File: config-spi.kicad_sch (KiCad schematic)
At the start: 38 parts, among them J4 0878311420, Q6 BSS138APW, Q7 BSS138APW, U3 XC7K70T-FBG484, U5 S25FL128LAGNFA010

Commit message: Loclib
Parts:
- U5: footprint antmicro-footprints:S25FL128SAGNFI000 -> lpddr4-test-board-footprints:S25FL128SAGNFI000; symbol antmicroMemory:S25FL128LAGNFA010 -> lpddr4-test-board:S25FL128LAGNFA010
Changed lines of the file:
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@@
     )
     (property "Value" "GND" (id 1) (at 23.622 262.2042 0))
-    (property "Footprint" "" (id 2) (at 23.495 257.81 0)
+    (property "Footprint" "lpddr4-test-board-footprints:" (id 2) (at 23.495 257.81 0)
       (effects (font (size 1.27 1.27)) hide)
     )
@@
     )
     (property "Value" "GND" (id 1) (at 70.4342 258.318 0))
-    (property "Footprint" "" (id 2) (at 66.04 258.445 0)
+    (property "Footprint" "lpddr4-test-board-footprints:" (id 2) (at 66.04 258.445 0)
       (effects (font (size 1.27 1.27)) hide)
     )
@@
     )
     (property "Value" "GND" (id 1) (at 69.977 140.2842 0))
-    (property "Footprint" "" (id 2) (at 69.85 135.89 0)
+    (property "Footprint" "lpddr4-test-board-footprints:" (id 2) (at 69.85 135.89 0)
       (effects (font (size 1.27 1.27)) hide)
     )
@@
     )
     (property "Value" "GND" (id 1) (at 235.5342 232.918 0))
-    (property "Footprint" "" (id 2) (at 231.14 233.045 0)
+    (property "Footprint" "lpddr4-test-board-footprints:" (id 2) (at 231.14 233.045 0)
       (effects (font (size 1.27 1.27)) hide)
     )
@@
     )
     (property "Value" "GND" (id 1) (at 235.5342 245.618 0))
-    (property "Footprint" "" (id 2) (at 231.14 245.745 0)
+    (property "Footprint" "lpddr4-test-board-footprints:" (id 2) (at 231.14 245.745 0)
       (effects (font (size 1.27 1.27)) hide)
     )
@@
     )
     (property "Value" "GND" (id 1) (at 166.3192 239.268 0))
-    (property "Footprint" "" (id 2) (at 161.925 239.395 0)
+    (property "Footprint" "lpddr4-test-board-footprints:" (id 2) (at 161.925 239.395 0)
       (effects (font (size 1.27 1.27)) hide)
     )
@@
     )
     (property "Value" "GND" (id 1) (at 166.9542 258.953 0))
-    (property "Footprint" "" (id 2) (at 162.56 259.08 0)
+    (property "Footprint" "lpddr4-test-board-footprints:" (id 2) (at 162.56 259.08 0)
       (effects (font (size 1.27 1.27)) hide)
     )
@@
     )
     (property "Value" "GND" (id 1) (at 249.047 174.5742 0))
-    (property "Footprint" "" (id 2) (at 248.92 170.18 0)
+    (property "Footprint" "lpddr4-test-board-footprints:" (id 2) (at 248.92 170.18 0)
       (effects (font (size 1.27 1.27)) hide)
     )
@@
     )
     (property "Value" "GND" (id 1) (at 156.972 179.0192 0))
-    (property "Footprint" "" (id 2) (at 156.845 174.625 0)
+    (property "Footprint" "lpddr4-test-board-footprints:" (id 2) (at 156.845 174.625 0)
       (effects (font (size 1.27 1.27)) hide)
     )
@@
     )
     (property "Value" "GND" (id 1) (at 236.1692 260.858 0))
-    (property "Footprint" "" (id 2) (at 231.775 260.985 0)
+    (property "Footprint" "lpddr4-test-board-footprints:" (id 2) (at 231.775 260.985 0)
       (effects (font (size 1.27 1.27)) hide)
     )
@@
     )
     (property "Value" "GND" (id 1) (at 282.067 182.1942 0))
-    (property "Footprint" "" (id 2) (at 281.94 177.8 0)
+    (property "Footprint" "lpddr4-test-board-footprints:" (id 2) (at 281.94 177.8 0)
       (effects (font (size 1.27 1.27)) hide)
     )
@@
     )
     (property "Value" "GND" (id 1) (at 133.477 141.5542 0))
-    (property "Footprint" "" (id 2) (at 133.35 137.16 0)
+    (property "Footprint" "lpddr4-test-board-footprints:" (id 2) (at 133.35 137.16 0)
       (effects (font (size 1.27 1.27)) hide)
     )
@@
     )
     (property "Value" "GND" (id 1) (at 376.047 129.4892 0))
-    (property "Footprint" "" (id 2) (at 375.92 125.095 0)
+    (property "Footprint" "lpddr4-test-board-footprints:" (id 2) (at 375.92 125.095 0)
       (effects (font (size 1.27 1.27)) hide)
     )
@@
     )
     (property "Value" "GND" (id 1) (at 61.722 113.6142 0))
-    (property "Footprint" "" (id 2) (at 61.595 109.22 0)
+    (property "Footprint" "lpddr4-test-board-footprints:" (id 2) (at 61.595 109.22 0)
       (effects (font (size 1.27 1.27)) hide)
     )
@@
     (pin "1")
   )
-  (symbol (lib_id "antmicroMemory:S25FL128LAGNFA010") (at 109.22 105.41 0) (mirror y) (unit 1)
+  (symbol (lib_id "lpddr4-test-board:S25FL128LAGNFA010") (at 109.22 105.41 0) (mirror y) (unit 1)
     (in_bom yes) (on_board yes) (fields_autoplaced)
     (property "Reference" "U5" (id 0) (at 91.44 98.7859 0)
@@
       (effects (font (size 1.524 1.524)))
     )
-    (property "Footprint" "antmicro-footprints:S25FL128SAGNFI000" (id 2) (at 90.805 144.78 0)
-      (effects (font (size 1.524 1.524)) hide)
-    )
+    (property "Footprint" "lpddr4-test-board-footprints:S25FL128SAGNFI000" (id 2) (at 90.805 144.78 0)
+      (effects (font (size 1.524 1.524)) hide)
+    )

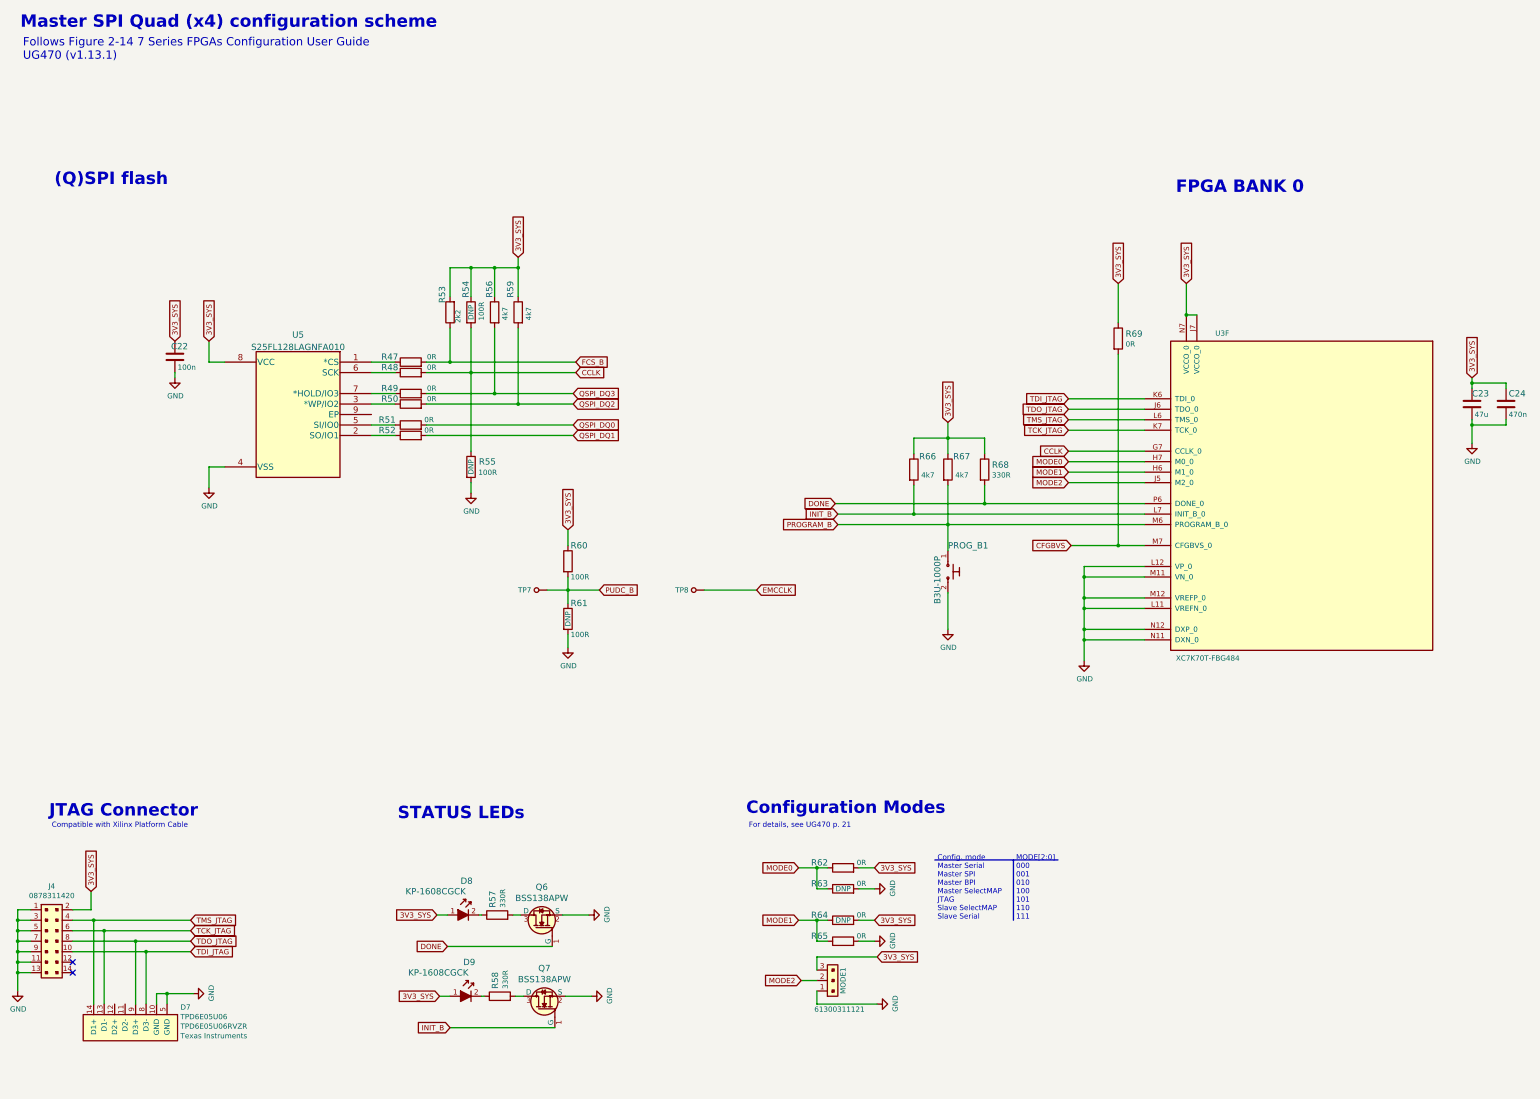
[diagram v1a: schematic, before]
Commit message: Introduce standardized components
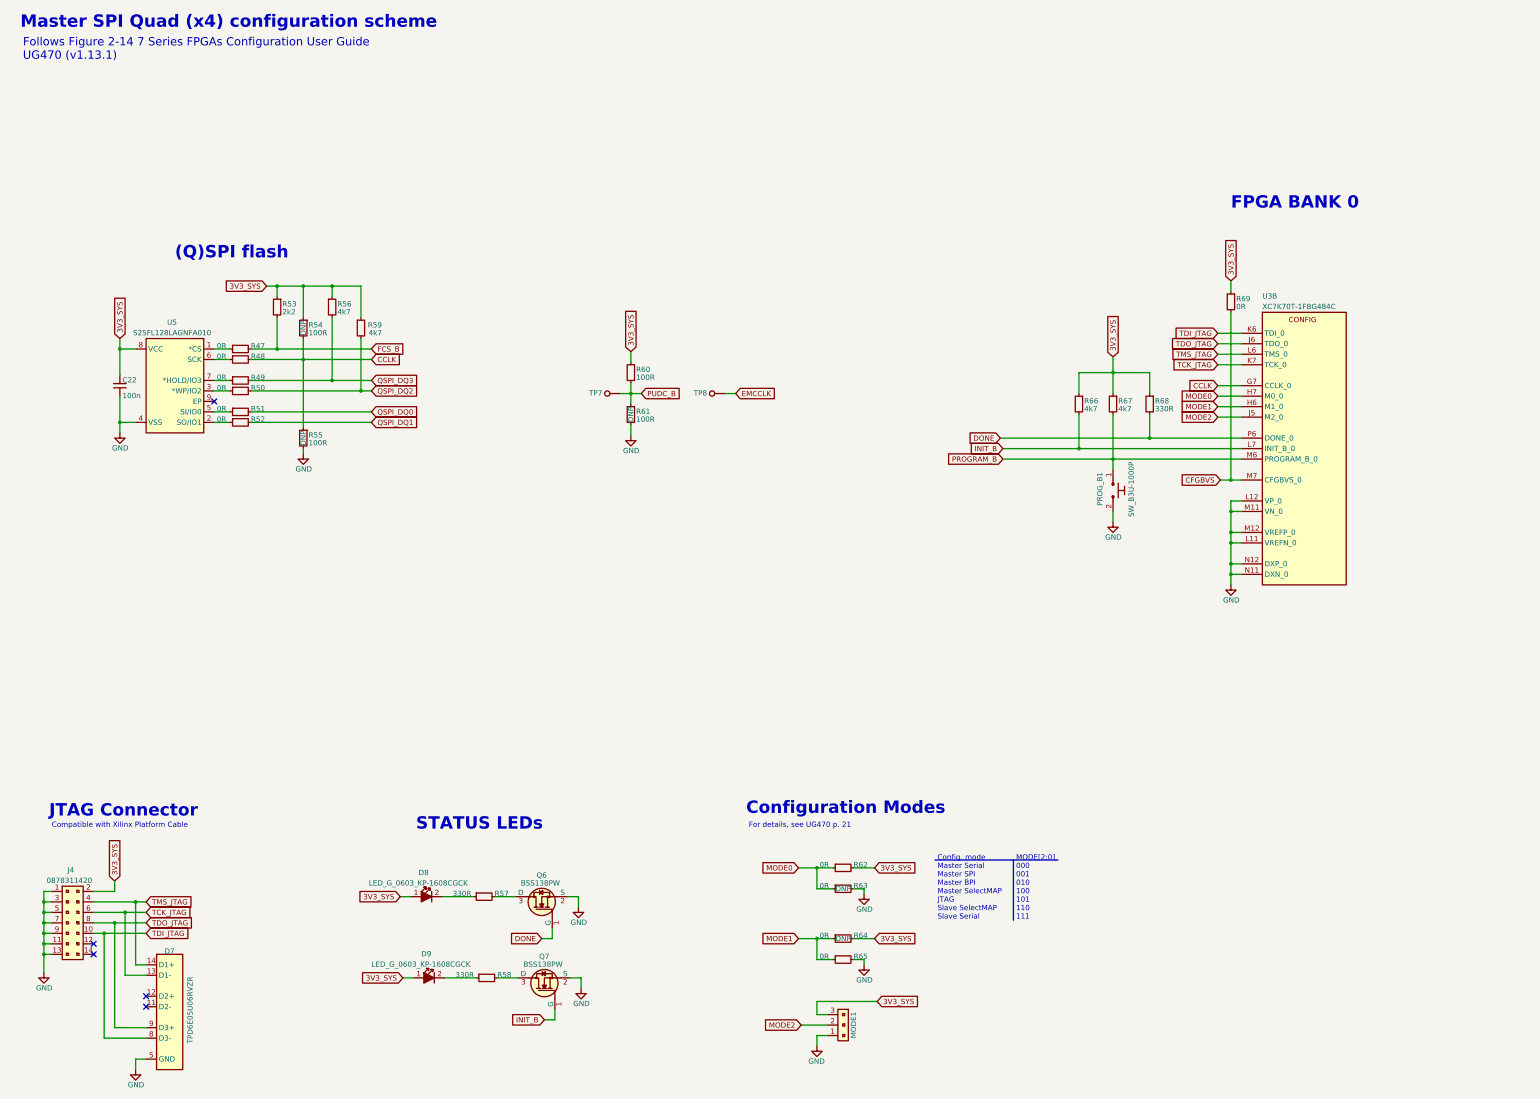
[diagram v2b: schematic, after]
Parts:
- removed C23: C_47u_0603, lpddr4-test-board-footprints:0603-cap, symbol lpddr4-test-board:C_47u_0603
- removed C24: C_470n_0402, lpddr4-test-board-footprints:0402-cap, symbol lpddr4-test-board:C_470n_0402
- removed U3: XC7K70T-FBG484, lpddr4-test-board-footprints:BGA484C100P22X22_2300X2300X244N, symbol lpddr4-test-board:XC7K70T-FBG484
- added U3: XC7K70T-FBG484, lpddr4-test-board-footprints:BGA484C100P22X22_2300X2300X244N, symbol lpddr4-test-board:XC7K70T-FBG484
- C22: value C_100n_0402_6V3 -> C_100n_6V3_0402; footprint lpddr4-test-board-footprints:0402-cap -> lpddr4-test-board-footprints:C_0402_1005Metric; symbol lpddr4-test-board:C_100n_0402_6V3 -> lpddr4-test-board:C_100n_6V3_0402; Author (none) -> Antmicro; License (none) -> Apache-2.0
- D7: value TPD6E05U06 -> TPD6E05U06RVZR; footprint lpddr4-test-board-footprints:TPD6E05U06 -> lpddr4-test-board-footprints:USON-14_3.5X1.3X0.5mm_P0.5mm; symbol lpddr4-test-board:TPD6E05U06 -> lpddr4-test-board:TPD6E05U06RVZR; Author (none) -> Antmicro; License (none) -> Apache-2.0
- D8, D9: value KP-1608CGCK -> LED_G_0603_KP-1608CGCK; footprint lpddr4-test-board-footprints:LED_0603 -> lpddr4-test-board-footprints:LED_0603_1608Metric_G; symbol lpddr4-test-board:KP-1608CGCK -> lpddr4-test-board:LED_G_0603_KP-1608CGCK; Author (none) -> Antmicro; License (none) -> Apache-2.0; Manufacturer KINGBRIGHT -> Kingbright
- J4: value 0878311420 -> PinHeader_2x7_P2mm_Drill1mm_Shrouded; footprint lpddr4-test-board-footprints:PinHeader_2x7_P2mm_Drill1mm -> lpddr4-test-board-footprints:PinHeader_2x7_P2mm_Drill1mm_Shrouded; symbol lpddr4-test-board:0878311420 -> lpddr4-test-board:PinHeader_2x7_P2mm_Drill1mm_Shrouded; Author (none) -> Antmicro; License (none) -> Apache-2.0
- MODE1: value 61300311121 -> PinHeader_1x3_P2.54mm_Drill1.1mm; symbol lpddr4-test-board:61300311121 -> lpddr4-test-board:PinHeader_1x3_P2.54mm_Drill1.1mm; Author (none) -> Antmicro; License (none) -> Apache-2.0; Manufacturer Wurth Electronics Inc. -> Würth Elektronik
- PROG_B1: value B3U-1000P -> SW_B3U-1000P; footprint lpddr4-test-board-footprints:Switch_Tactile_SMD_B3U-1000P -> lpddr4-test-board-footprints:SW_B3U-3000P; symbol lpddr4-test-board:B3U-1000P -> lpddr4-test-board:SW_B3U-1000P; Author (none) -> Antmicro; License (none) -> Apache-2.0; Manufacturer Omron Electronics Inc-EMC Div -> Omron Electronics
- Q6, Q7: value BSS138APW -> BSS138PW; symbol lpddr4-test-board:BSS138APW -> lpddr4-test-board:BSS138PW; Author (none) -> Antmicro; License (none) -> Apache-2.0; Manufacturer ON Semiconductor -> Nexperia
- R47, R48, R49, R50, R51, R52, R62, R63, R64, R65, R69: footprint lpddr4-test-board-footprints:0402-res -> lpddr4-test-board-footprints:R_0402_1005Metric; Author (none) -> Antmicro; Current (none) -> 1A; License (none) -> Apache-2.0; Manufacturer PANASONIC -> Panasonic
- R53: footprint lpddr4-test-board-footprints:0402-res -> lpddr4-test-board-footprints:R_0402_1005Metric; Author (none) -> Antmicro; License (none) -> Apache-2.0; MPN RC0402FR-072K2L -> CR0402-FX-2201GLF; Manufacturer YAGEO -> Bourns; Tolerance (none) -> 1%
- R54, R55, R60, R61: footprint lpddr4-test-board-footprints:0402-res -> lpddr4-test-board-footprints:R_0402_1005Metric; Author (none) -> Antmicro; License (none) -> Apache-2.0; Manufacturer BOURNS -> Bourns; Tolerance (none) -> 1%
- R56, R59, R66, R67: footprint lpddr4-test-board-footprints:0402-res -> lpddr4-test-board-footprints:R_0402_1005Metric; Author (none) -> Antmicro; License (none) -> Apache-2.0; MPN ERJ2GEJ472X -> CR0402-FX-4701GLF; Manufacturer PANASONIC_ELECTRONIC_COMPONENTS -> Bourns; Tolerance (none) -> 1%
- R57, R58, R68: footprint lpddr4-test-board-footprints:0402-res -> lpddr4-test-board-footprints:R_0402_1005Metric; Author (none) -> Antmicro; License (none) -> Apache-2.0; MPN MCMR04X3300FTL -> CR0402-FX-3300GLF; Manufacturer MULTICOMP -> Bourns; Tolerance (none) -> 1%
- TP7, TP8: value TP_SMD1MM -> TP_1mm_SMD; symbol lpddr4-test-board:TP_SMD1MM -> lpddr4-test-board:TP_1mm_SMD; Author (none) -> Antmicro; License (none) -> Apache-2.0
- U5: footprint lpddr4-test-board-footprints:S25FL128SAGNFI000 -> lpddr4-test-board-footprints:WSON-8_6x8x0.5mm_P1.27mm; Author (none) -> Antmicro; License (none) -> Apache-2.0; MPN S25FL128SAGNFI000 -> S25FL128LAGNFA010
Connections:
- net 3V3_SYS: now also C22.2, R53.1; no longer C22.1, R53.2
- net CCLK: now also U3.G7 (CCLK_0)
- net CFGBVS: now also U3.M7 (CFGBVS_0)
- net DONE: now also U3.P6 (DONE_0)
- net FCS_B: now also R53.2; no longer R53.1
- net GND: now also C22.1, U3.L11 (VREFN_0), U3.L12 (VP_0), U3.M11 (VN_0), U3.M12 (VREFP_0), U3.N11 (DXN_0), U3.N12 (DXP_0); no longer C22.2
- net INIT_B: now also U3.L7 (INIT_B_0)
- net MODE0: now also U3.H7 (M0_0)
- net MODE1: now also U3.H6 (M1_0)
- net MODE2: now also U3.J5 (M2_0)
- net PROGRAM_B: now also U3.M6 (PROGRAM_B_0)
- net TCK_JTAG: now also D7.2 (D1-), U3.K7 (TCK_0)
- net TDI_JTAG: now also D7.7 (D3-), U3.K6 (TDI_0)
- net TDO_JTAG: now also D7.6 (D3+), U3.J6 (TDO_0)
- net TMS_JTAG: now also D7.1 (D1+), U3.L6 (TMS_0)
- net at D7.11 (D2-): now also D7.4 (D2-)
- net at D7.12 (D2+): now also D7.3 (D2+)
- no-connect marks 2 -> 5
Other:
- moved on the sheet: C22, J4, R47, R48, R49, R50, R51, R52, R53, R54, R55, R56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

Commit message: [#55158] components update
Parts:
- MODE1: footprint lpddr4-test-board-footprints:PinHeader_1x3_P2.54_Drill1.1mm -> lpddr4-test-board-footprints:PinHeader_1x3_P2.54mm_Drill1.1mm; VSD_class (none) -> IO Header
- PROG_B1: footprint lpddr4-test-board-footprints:SW_B3U-3000P -> antmicro-footprints:SW_B3U-1000P_SMD; symbol lpddr4-test-board:SW_B3U-1000P -> lpddr4-test-board:SW_B3U-1000P_SMD; Manufacturer Omron Electronics -> Omron
- R54, R55, R61, R63, R64: now not fitted; now left out of the parts list
- TP7, TP8: footprint lpddr4-test-board-footprints:Testpoint_smd_1mm -> antmicro-footprints:TP_SMD_1mm
- U3: Manufacturer Xilinx -> AMD-Xilinx
